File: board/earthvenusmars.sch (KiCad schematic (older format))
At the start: 27 parts, among them J1 Conn_01x05_Female, J2 Conn_01x02_Female, J4 Conn_01x05, SW1 SW_SPST, SW2 SW_SPST, SW3 SW_SPST, U1 ATSAMD21G18A-AU, U2 MIC5504-3.3YM5, Y1 32768Hz

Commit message: adopt v2 programmer pins on EVM board
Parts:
- J1: footprint Pad_SMD:Pad_SMD_1.27mm_01x05 -> earthvenusmars:programmer_pads_v2
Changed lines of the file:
@@
 F 0 "J1" V 4500 4800 50  0000 L CNN
 F 1 "Conn_01x05_Female" V 4650 4500 50  0000 L CNN
-F 2 "Pad_SMD:Pad_SMD_1.27mm_01x05" H 4600 5000 50  0001 C CNN
+F 2 "earthvenusmars:programmer_pads_v2" H 4600 5000 50  0001 C CNN
 F 3 "~" H 4600 5000 50  0001 C CNN
 	1    4600 5000

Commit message: change usb port footprint to 4-pin 2.54mm. I still don't like my options for using a usb micro port on the back. not that glue is any better...
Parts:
- removed J2: Conn_01x02_Female, Pad_SMD:Pad_SMD_1.27mm_01x02, symbol Connector:Conn_01x02_Female
- J4: value Conn_01x05 -> Conn_01x04; footprint Connector_PinHeader_1.27mm:PinHeader_1x05_P1.27mm_Vertical -> Connector_PinHeader_2.54mm:PinHeader_1x04_P2.54mm_Vertical; symbol Connector_Generic:Conn_01x05 -> Connector_Generic:Conn_01x04
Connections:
- wire segments 84 -> 81
- no-connect marks 24 -> 23
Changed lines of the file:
@@
 L power:GND #PWR0102
 U 1 1 5EB2B290
-P 3800 4550
-F 0 "#PWR0102" H 3800 4300 50  0001 C CNN
-F 1 "GND" V 3805 4422 50  0000 R CNN
-F 2 "" H 3800 4550 50  0001 C CNN
-F 3 "" H 3800 4550 50  0001 C CNN
-	1    3800 4550
+P 3700 4550
+F 0 "#PWR0102" H 3700 4300 50  0001 C CNN
+F 1 "GND" V 3705 4422 50  0000 R CNN
+F 2 "" H 3700 4550 50  0001 C CNN
+F 3 "" H 3700 4550 50  0001 C CNN
+	1    3700 4550
 	-1   0    0    1
 $EndComp
@@
 	5400 1750 5500 1750
 $Comp
-L Connector_Generic:Conn_01x05 J4
+L Connector_Generic:Conn_01x04 J4
 U 1 1 5F9E60C8
 P 3600 4750
 F 0 "J4" V 3564 4462 50  0000 R CNN
-F 1 "Conn_01x05" V 3700 4950 50  0000 R CNN
-F 2 "Connector_PinHeader_1.27mm:PinHeader_1x05_P1.27mm_Vertical" H 3600 4750 50  0001 C CNN
+F 1 "Conn_01x04" V 3700 4950 50  0000 R CNN
+F 2 "Connector_PinHeader_2.54mm:PinHeader_1x04_P2.54mm_Vertical" H 3600 4750 50  0001 C CNN
 F 3 "~" H 3600 4750 50  0001 C CNN
 	1    3600 4750
@@
 	3050 3750 3050 3550
 Wire Wire Line
-	3050 3550 3250 3550
-Wire Wire Line
 	2850 3550 2850 3750
 Wire Wire Line
@@
 SWCLK
 $Comp
-L Connector:Conn_01x02_Female J2
-U 1 1 5FC334AA
-P 3150 3200
-F 0 "J2" V 3088 3012 50  0000 R CNN
-F 1 "Conn_01x02_Female" V 3200 3450 50  0000 R CNN
-F 2 "Pad_SMD:Pad_SMD_1.27mm_01x02" H 3150 3200 50  0001 C CNN
-F 3 "~" H 3150 3200 50  0001 C CNN
-	1    3150 3200
-	0    -1   -1   0
-$EndComp
-Wire Wire Line
-	3150 3650 3150 3400
-Connection ~ 3150 3650
-Wire Wire Line
-	3250 3550 3250 3400
-Connection ~ 3250 3550
-Wire Wire Line
-	3250 3550 3950 3550
-$Comp
 L power:GND #PWR0138
 U 1 1 5FC4F9CF
@@
 Wire Wire Line
 	3600 4150 3950 4150
-NoConn ~ 3700 4550
+Wire Wire Line
+	3050 3550 3950 3550
 $EndSCHEMATC

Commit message: concept for smd usb pads on bottom of board + a pass at the shell case cable management for that
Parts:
- J4: footprint Connector_PinHeader_2.54mm:PinHeader_1x04_P2.54mm_Vertical -> earthvenusmars:USB_SMD
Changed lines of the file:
@@
 F 0 "J4" V 3564 4462 50  0000 R CNN
 F 1 "Conn_01x04" V 3700 4950 50  0000 R CNN
-F 2 "Connector_PinHeader_2.54mm:PinHeader_1x04_P2.54mm_Vertical" H 3600 4750 50  0001 C CNN
+F 2 "earthvenusmars:USB_SMD" H 3600 4750 50  0001 C CNN
 F 3 "~" H 3600 4750 50  0001 C CNN
 	1    3600 4750

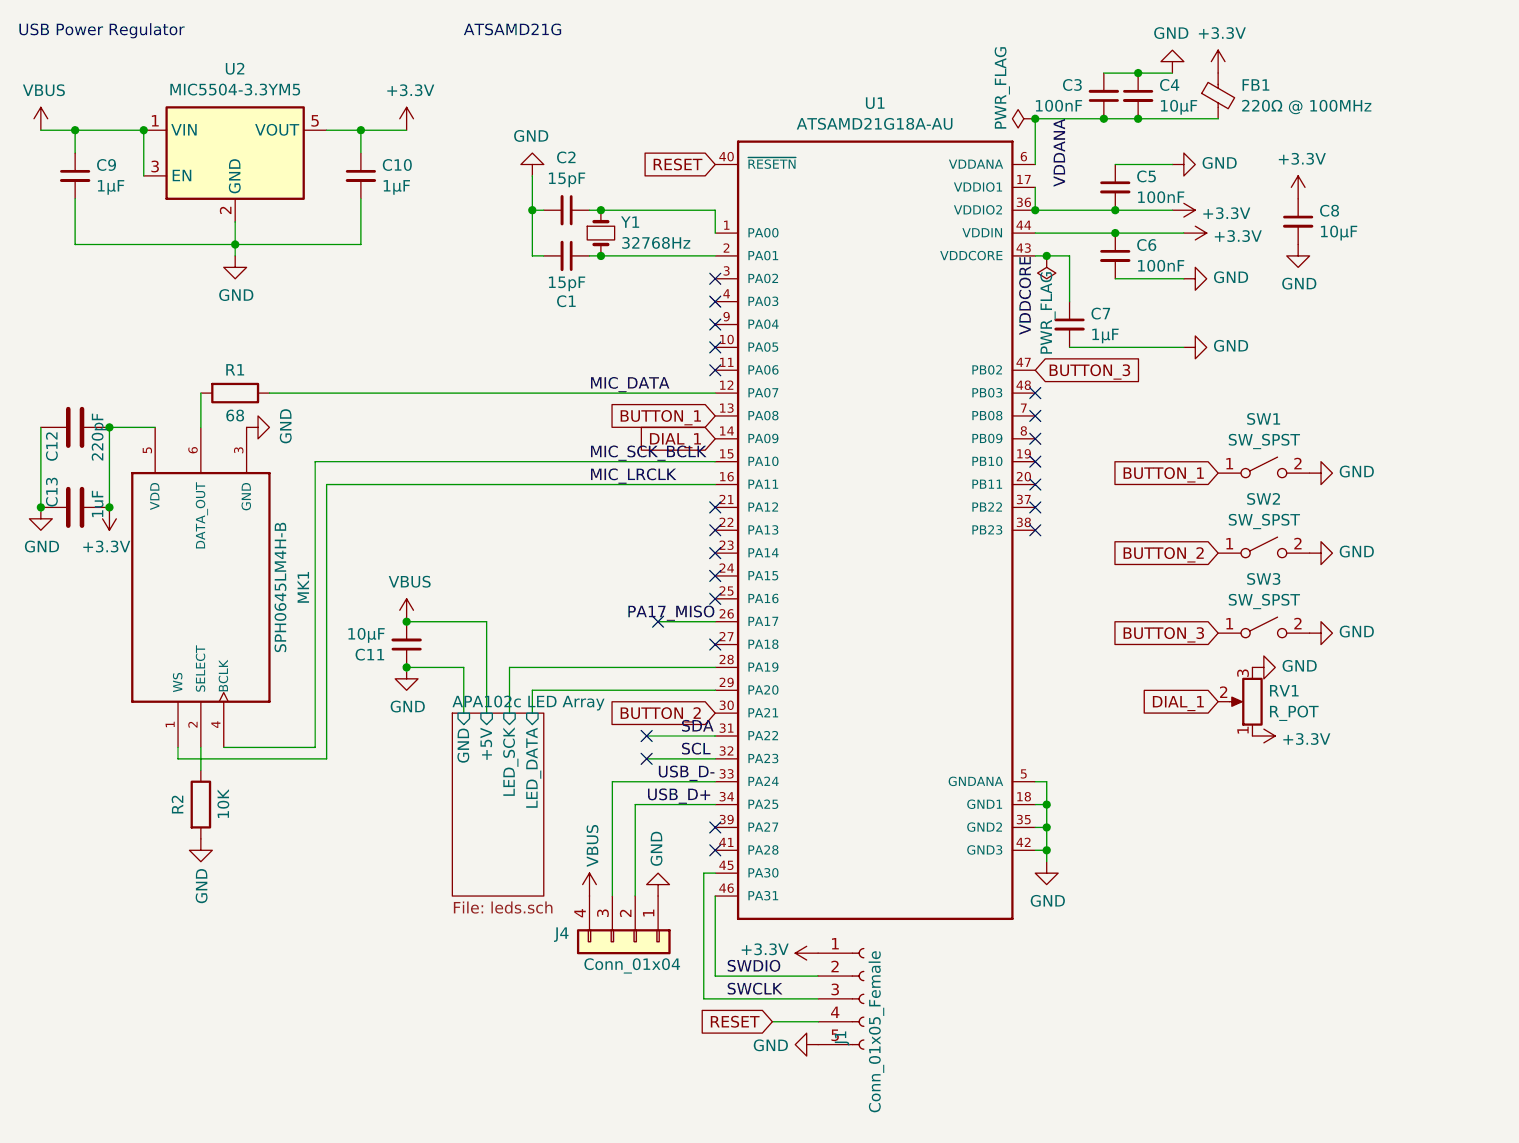
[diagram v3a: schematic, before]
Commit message: new plan for spoke buttons: touch buttons. schematic changes for new button layout; add footprints for new touch buttons; rewire new and existing buttons; re-layout linreg and power circuity for better spacing
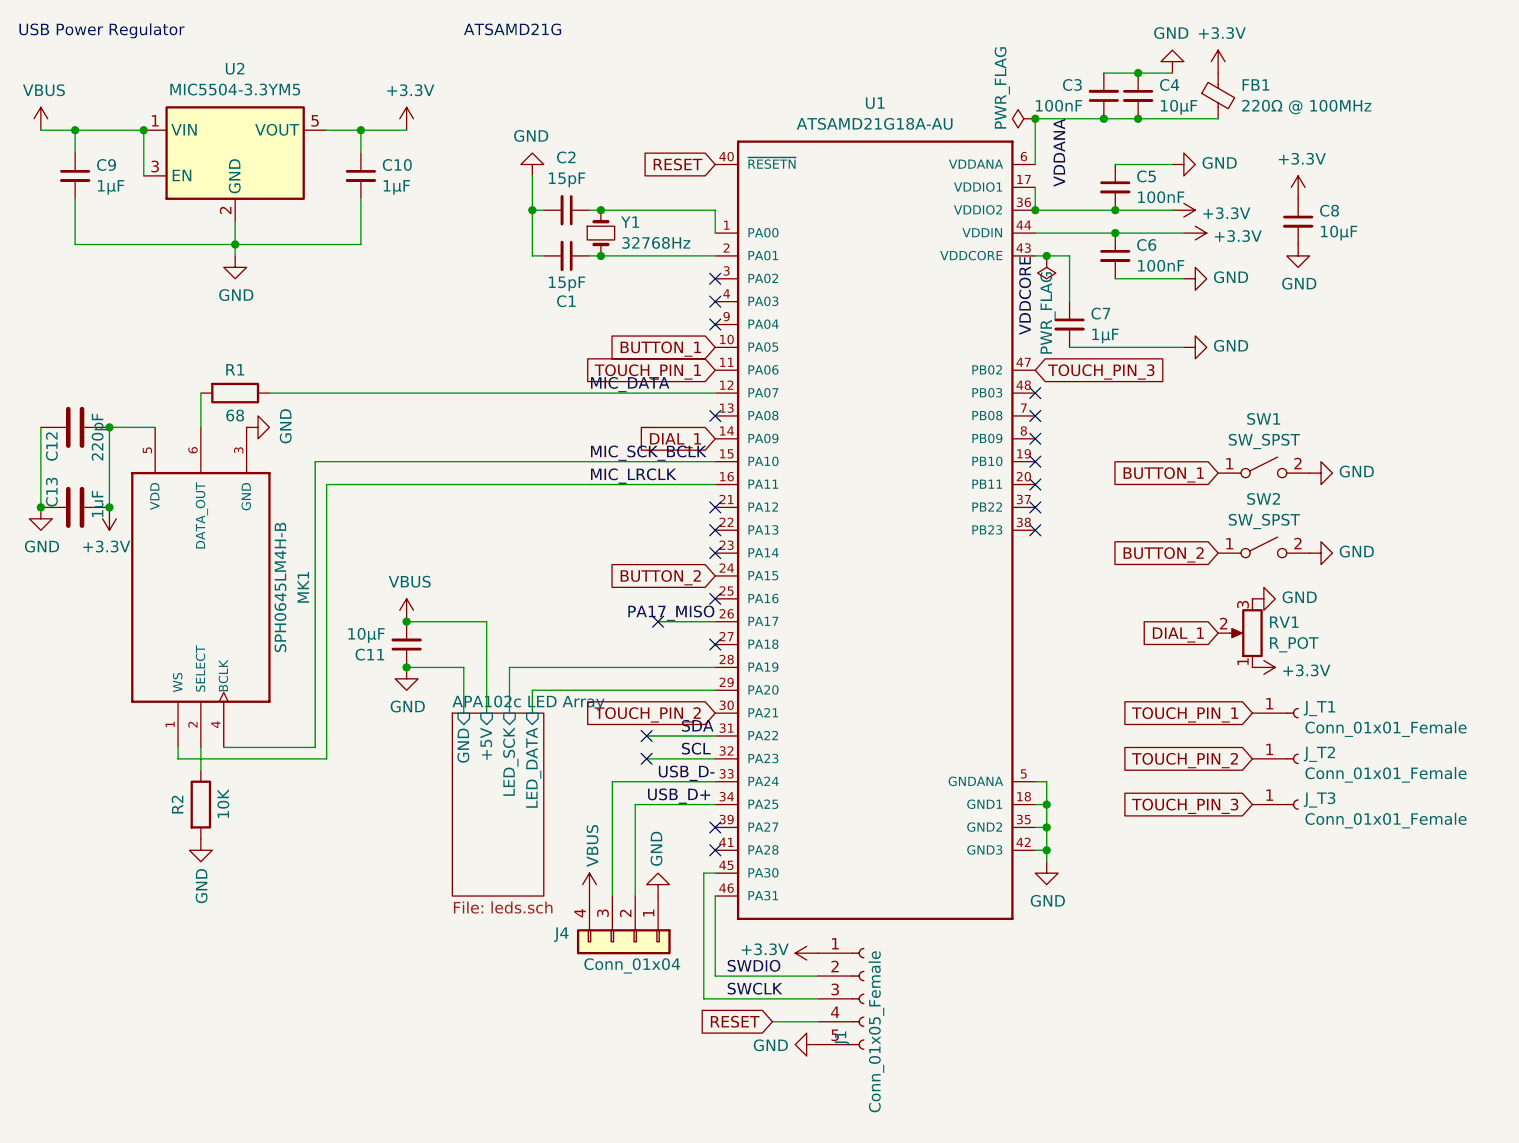
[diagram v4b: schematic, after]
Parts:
- removed SW3: SW_SPST, Button_Switch_SMD:KMR731NG_LFS, symbol Switch:SW_SPST
- added J_T1: Conn_01x01_Female, earthvenusmars:touch_earth, symbol Connector:Conn_01x01_Female
- added J_T2: Conn_01x01_Female, earthvenusmars:touch_venus, symbol Connector:Conn_01x01_Female
- added J_T3: Conn_01x01_Female, earthvenusmars:touch_mars, symbol Connector:Conn_01x01_Female
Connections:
- net BUTTON_1: now also U1.10 (PA05); no longer U1.13 (PA08)
- net BUTTON_2: now also U1.24 (PA15); no longer U1.30 (PA21)
- net TOUCH_PIN_1: now reaches U1.11 (PA06)
- net TOUCH_PIN_1: now also J_T1.1 (Pin_1)
- net BUTTON_3 renamed TOUCH_PIN_3
- net TOUCH_PIN_3: now also J_T3.1 (Pin_1)
- new net TOUCH_PIN_2: J_T2.1 (Pin_1), U1.30 (PA21)
- no-connect marks 23 -> 21
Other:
- moved on the sheet: RV1
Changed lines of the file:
@@
 Text Label 3950 4050 2    50   ~ 0
 USB_D-
-NoConn ~ 3950 3150
 NoConn ~ 3950 3050
 NoConn ~ 3950 2950
 NoConn ~ 3950 2850
-NoConn ~ 3950 2250
-NoConn ~ 3950 2150
 NoConn ~ 3950 2050
 NoConn ~ 3950 1950
@@
 $EndComp
 $Comp
-L Switch:SW_SPST SW3
-U 1 1 5F910AB5
-P 6350 3400
-F 0 "SW3" H 6350 3635 50  0000 C CNN
-F 1 "SW_SPST" H 6350 3544 50  0000 C CNN
-F 2 "Button_Switch_SMD:KMR731NG_LFS" H 6350 3400 50  0001 C CNN
-F 3 "~" H 6350 3400 50  0001 C CNN
-F 4 "KMR731NGLFS" H 6350 3400 50  0001 C CNN "Designation"
-	1    6350 3400
-	1    0    0    -1
-$EndComp
-$Comp
 L power:GND #PWR0133
 U 1 1 5F9110A0
@@
 L power:GND #PWR0135
 U 1 1 5F9113D1
-P 6300 3550
-F 0 "#PWR0135" H 6300 3300 50  0001 C CNN
-F 1 "GND" V 6305 3422 50  0000 R CNN
-F 2 "" H 6300 3550 50  0001 C CNN
-F 3 "" H 6300 3550 50  0001 C CNN
-	1    6300 3550
-	0    -1   -1   0
-$EndComp
-Text GLabel 3950 2450 0    50   Input ~ 0
+P 6300 3250
+F 0 "#PWR0135" H 6300 3000 50  0001 C CNN
+F 1 "GND" V 6305 3122 50  0000 R CNN
+F 2 "" H 6300 3250 50  0001 C CNN
+F 3 "" H 6300 3250 50  0001 C CNN
+	1    6300 3250
+	0    -1   -1   0
+$EndComp
+Text GLabel 3950 2150 0    50   Input ~ 0
 BUTTON_1
-Text GLabel 3950 3750 0    50   Input ~ 0
+Text GLabel 3950 3150 0    50   Input ~ 0
 BUTTON_2
-Text GLabel 5350 2250 2    50   Input ~ 0
-BUTTON_3
-Text GLabel 6150 3400 0    50   Input ~ 0
-BUTTON_3
 Text GLabel 6150 3050 0    50   Input ~ 0
 BUTTON_2
@@
 L Device:R_POT RV1
 U 1 1 5FA0CDD3
-P 6300 3700
-F 0 "RV1" H 6230 3654 50  0000 R CNN
-F 1 "R_POT" H 6230 3745 50  0000 R CNN
-F 2 "Pot_dial_3352T-1-103LF:Pot_dial_3352T-1-103LF" H 6300 3700 50  0001 C CNN
-F 3 "~" H 6300 3700 50  0001 C CNN
-	1    6300 3700
+P 6300 3400
+F 0 "RV1" H 6230 3354 50  0000 R CNN
+F 1 "R_POT" H 6230 3445 50  0000 R CNN
+F 2 "Pot_dial_3352T-1-103LF:Pot_dial_3352T-1-103LF" H 6300 3400 50  0001 C CNN
+F 3 "~" H 6300 3400 50  0001 C CNN
+	1    6300 3400
 	-1   0    0    1
 $EndComp
 Text GLabel 3950 2550 0    50   Input ~ 0
 DIAL_1
-Text GLabel 6150 3700 0    50   Input ~ 0
+Text GLabel 6150 3400 0    50   Input ~ 0
 DIAL_1
 $Comp
 L power:+3.3V #PWR0136
 U 1 1 5FBE3505
-P 6300 3850
-F 0 "#PWR0136" H 6300 3700 50  0001 C CNN
-F 1 "+3.3V" V 6315 3978 50  0000 L CNN
-F 2 "" H 6300 3850 50  0001 C CNN
-F 3 "" H 6300 3850 50  0001 C CNN
-	1    6300 3850
+P 6300 3550
+F 0 "#PWR0136" H 6300 3400 50  0001 C CNN
+F 1 "+3.3V" V 6315 3678 50  0000 L CNN
+F 2 "" H 6300 3550 50  0001 C CNN
+F 3 "" H 6300 3550 50  0001 C CNN
+	1    6300 3550
 	0    1    1    0
 $EndComp
@@
 	1    4600 5000
 	1    0    0    -1
-$EndComp
-$Comp
-L power:GND #PWR0137
-U 1 1 5FBFE728
-P 6550 3400
-F 0 "#PWR0137" H 6550 3150 50  0001 C CNN
-F 1 "GND" V 6555 3272 50  0000 R CNN
-F 2 "" H 6550 3400 50  0001 C CNN
-F 3 "" H 6550 3400 50  0001 C CNN
-	1    6550 3400
-	0    -1   -1   0
 $EndComp
 $Comp
@@
 Wire Wire Line
 	3050 3550 3950 3550
+Text GLabel 3950 2250 0    50   Input ~ 0
+TOUCH_PIN_1
+NoConn ~ 3950 2450
+Text GLabel 3950 3750 0    50   Input ~ 0
+TOUCH_PIN_2
+Text GLabel 6300 3950 0    50   Input ~ 0
+TOUCH_PIN_2
+Text GLabel 6300 4150 0    50   Input ~ 0
+TOUCH_PIN_3
+$Comp
+L Connector:Conn_01x01_Female J_T2
+U 1 1 60BC2291
+P 6500 3950
+F 0 "J_T2" H 6528 3976 50  0000 L CNN
+F 1 "Conn_01x01_Female" H 6528 3885 50  0000 L CNN
+F 2 "earthvenusmars:touch_venus" H 6500 3950 50  0001 C CNN
+F 3 "~" H 6500 3950 50  0001 C CNN
+	1    6500 3950
+	1    0    0    -1
+$EndComp
+$Comp
+L Connector:Conn_01x01_Female J_T3
+U 1 1 60BC3BD3
+P 6500 4150
+F 0 "J_T3" H 6528 4176 50  0000 L CNN
+F 1 "Conn_01x01_Female" H 6528 4085 50  0000 L CNN
+F 2 "earthvenusmars:touch_mars" H 6500 4150 50  0001 C CNN
+F 3 "~" H 6500 4150 50  0001 C CNN
+	1    6500 4150
+	1    0    0    -1
+$EndComp
+Text GLabel 6300 3750 0    50   Input ~ 0
+TOUCH_PIN_1
+$Comp
+L Connector:Conn_01x01_Female J_T1
+U 1 1 60BC9517
+P 6500 3750
+F 0 "J_T1" H 6528 3776 50  0000 L CNN
+F 1 "Conn_01x01_Female" H 6528 3685 50  0000 L CNN
+F 2 "earthvenusmars:touch_earth" H 6500 3750 50  0001 C CNN
+F 3 "~" H 6500 3750 50  0001 C CNN
+	1    6500 3750
+	1    0    0    -1
+$EndComp
+Text GLabel 5350 2250 2    50   Input ~ 0
+TOUCH_PIN_3
 $EndSCHEMATC

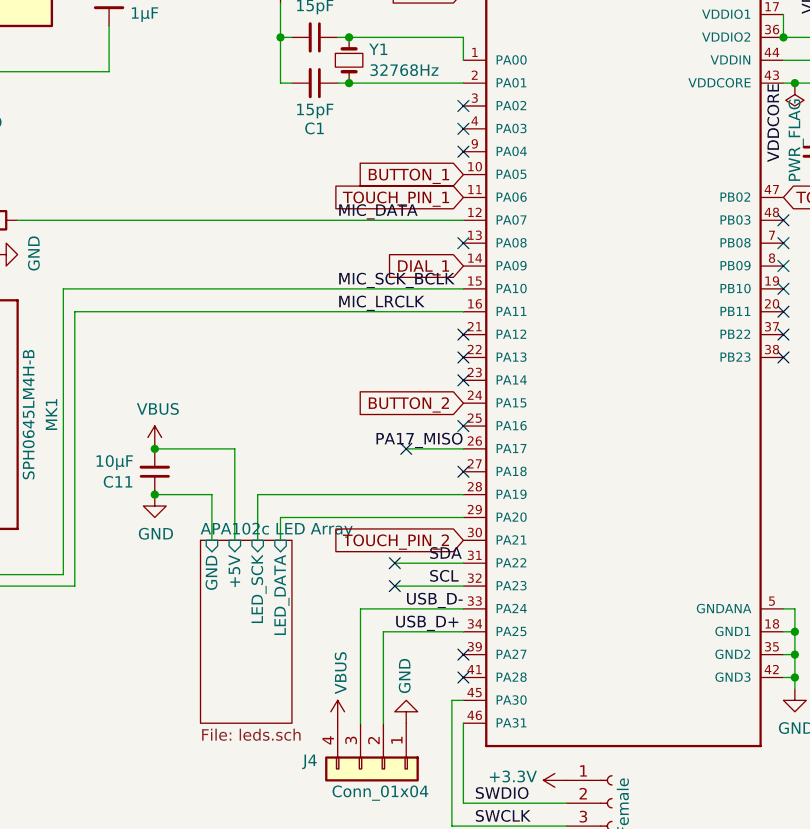
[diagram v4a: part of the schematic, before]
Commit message: reposition buttons farther away from touch buttons to avoid accidental touch + better overall spacing
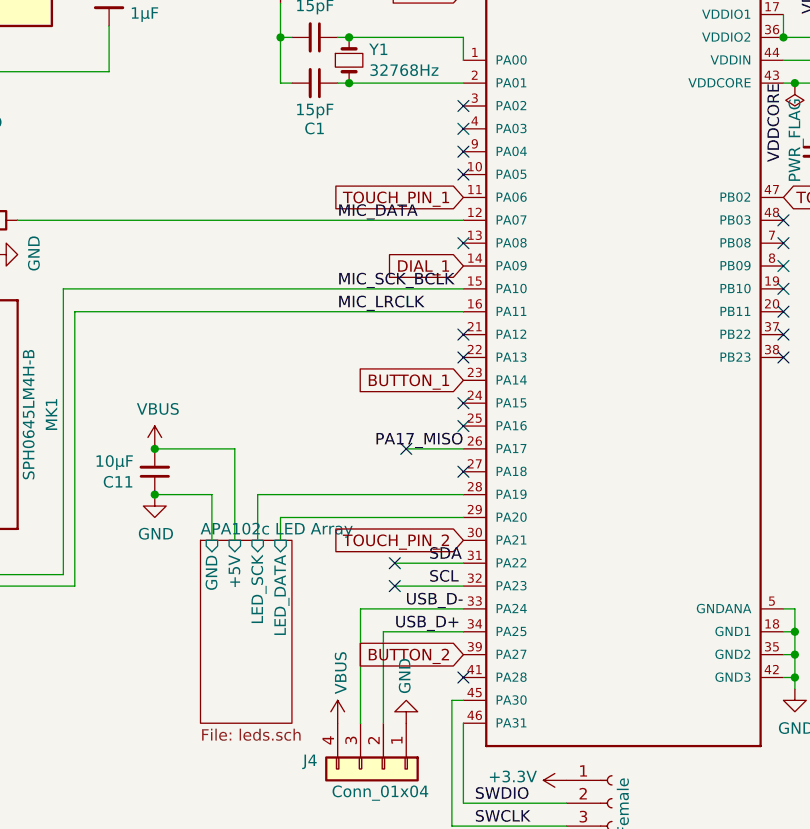
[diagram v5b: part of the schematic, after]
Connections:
- net BUTTON_1: now also U1.23 (PA14); no longer U1.10 (PA05)
- net BUTTON_2: now also U1.39 (PA27); no longer U1.24 (PA15)
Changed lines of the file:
@@
 Text Label 3950 4050 2    50   ~ 0
 USB_D-
-NoConn ~ 3950 3050
 NoConn ~ 3950 2950
 NoConn ~ 3950 2850
@@
 NoConn ~ 3950 3450
 NoConn ~ 3950 3250
-NoConn ~ 3950 4250
+NoConn ~ 3950 3150
 NoConn ~ 3950 4350
 Wire Wire Line
@@
 	0    -1   -1   0
 $EndComp
-Text GLabel 3950 2150 0    50   Input ~ 0
+Text GLabel 3950 3050 0    50   Input ~ 0
 BUTTON_1
-Text GLabel 3950 3150 0    50   Input ~ 0
+Text GLabel 3950 4250 0    50   Input ~ 0
 BUTTON_2
 Text GLabel 6150 3050 0    50   Input ~ 0
@@
 Text GLabel 5350 2250 2    50   Input ~ 0
 TOUCH_PIN_3
+NoConn ~ 3950 2150
 $EndSCHEMATC

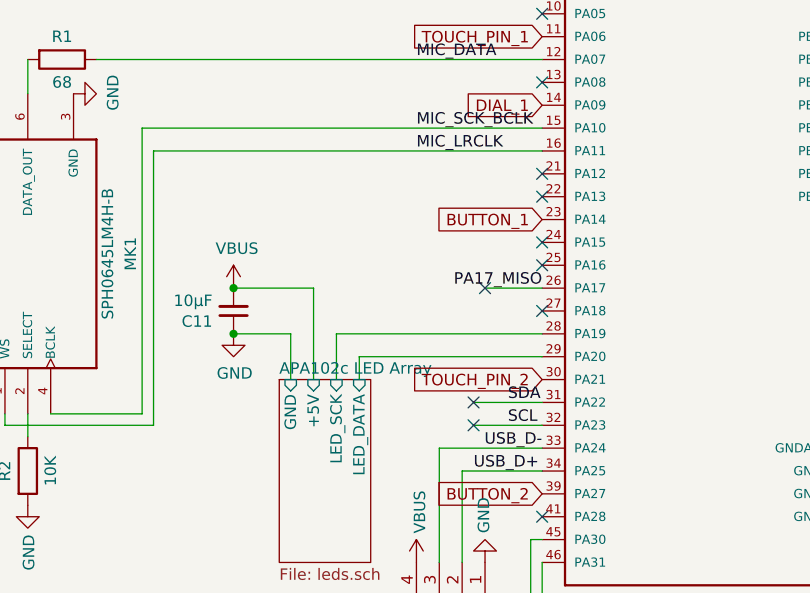
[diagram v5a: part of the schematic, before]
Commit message: add hackable ports for led spi & i2c for who knows what reason
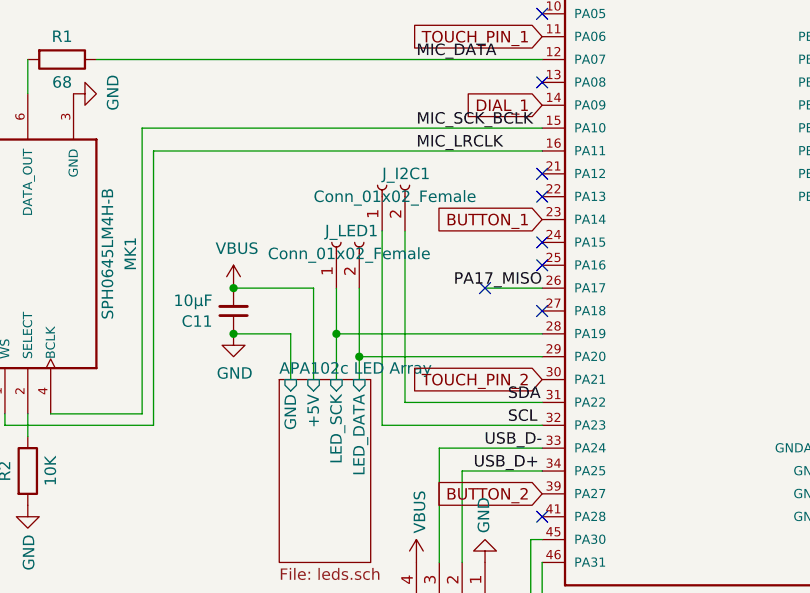
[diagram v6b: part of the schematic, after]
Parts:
- added J_I2C1, J_LED1: Conn_01x02_Female, earthvenusmars:SMD_Pad_01x02_1.27mm, symbol Connector:Conn_01x02_Female
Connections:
- net APA102c LED Array/LED_DATA: now also J_LED1.2 (Pin_2)
- net APA102c LED Array/LED_SCK: now also J_LED1.1 (Pin_1)
- net SCL: now also J_I2C1.1 (Pin_1)
- net SDA: now also J_I2C1.2 (Pin_2)
- no-connect marks 21 -> 19
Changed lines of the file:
@@
 $EndComp
 Connection ~ 5350 1550
-Wire Wire Line
-	3950 3950 3650 3950
-Wire Wire Line
-	3950 3850 3650 3850
 Text Label 3800 3850 0    50   ~ 0
 SDA
@@
 Wire Wire Line
 	2600 3350 2950 3350
-NoConn ~ 3650 3850
-NoConn ~ 3650 3950
 Wire Wire Line
 	1300 2500 1500 2500
@@
 TOUCH_PIN_3
 NoConn ~ 3950 2150
+$Comp
+L Connector:Conn_01x02_Female J_LED1
+U 1 1 60BA94AC
+P 3050 3150
+F 0 "J_LED1" V 3100 3200 50  0000 R CNN
+F 1 "Conn_01x02_Female" V 3000 3450 50  0000 R CNN
+F 2 "earthvenusmars:SMD_Pad_01x02_1.27mm" H 3050 3150 50  0001 C CNN
+F 3 "~" H 3050 3150 50  0001 C CNN
+	1    3050 3150
+	0    -1   -1   0
+$EndComp
+Wire Wire Line
+	3150 3350 3150 3650
+Connection ~ 3150 3650
+Wire Wire Line
+	3050 3350 3050 3550
+Connection ~ 3050 3550
+$Comp
+L Connector:Conn_01x02_Female J_I2C1
+U 1 1 60BB2E0D
+P 3250 2900
+F 0 "J_I2C1" V 3300 2900 50  0000 R CNN
+F 1 "Conn_01x02_Female" V 3200 3200 50  0000 R CNN
+F 2 "earthvenusmars:SMD_Pad_01x02_1.27mm" H 3250 2900 50  0001 C CNN
+F 3 "~" H 3250 2900 50  0001 C CNN
+	1    3250 2900
+	0    -1   -1   0
+$EndComp
+Wire Wire Line
+	3350 3850 3350 3100
+Wire Wire Line
+	3350 3850 3950 3850
+Wire Wire Line
+	3250 3100 3250 3950
+Wire Wire Line
+	3250 3950 3950 3950
 $EndSCHEMATC
